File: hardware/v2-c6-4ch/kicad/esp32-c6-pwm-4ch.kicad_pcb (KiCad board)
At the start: 2 copper layers, 90 x 70 mm, 40 parts, among them Q1 AO3400A, Q2 AO3400A, Q3 AO3400A, Q4 AO3400A

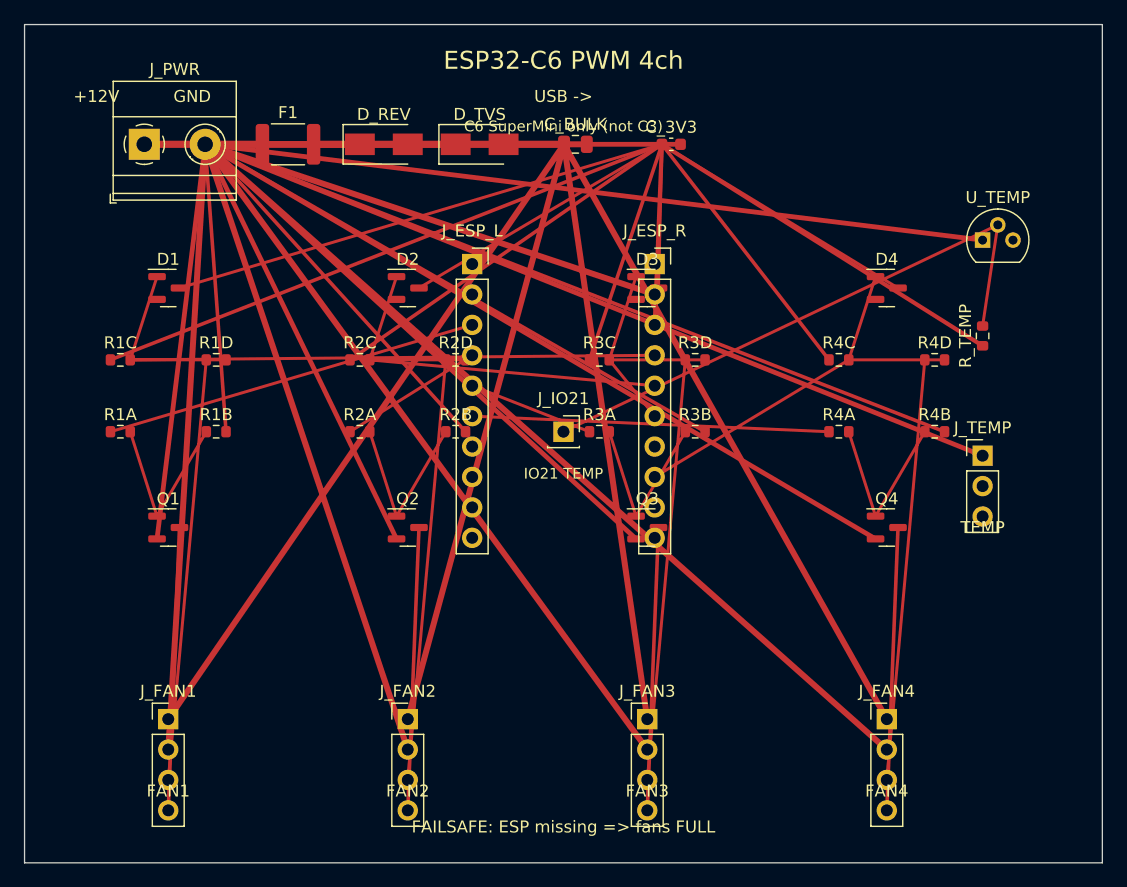
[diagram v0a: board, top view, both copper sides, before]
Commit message: no-mistakes(review): Sensorbus dokumentiert; vollständiges PCB-Routing bleibt offen
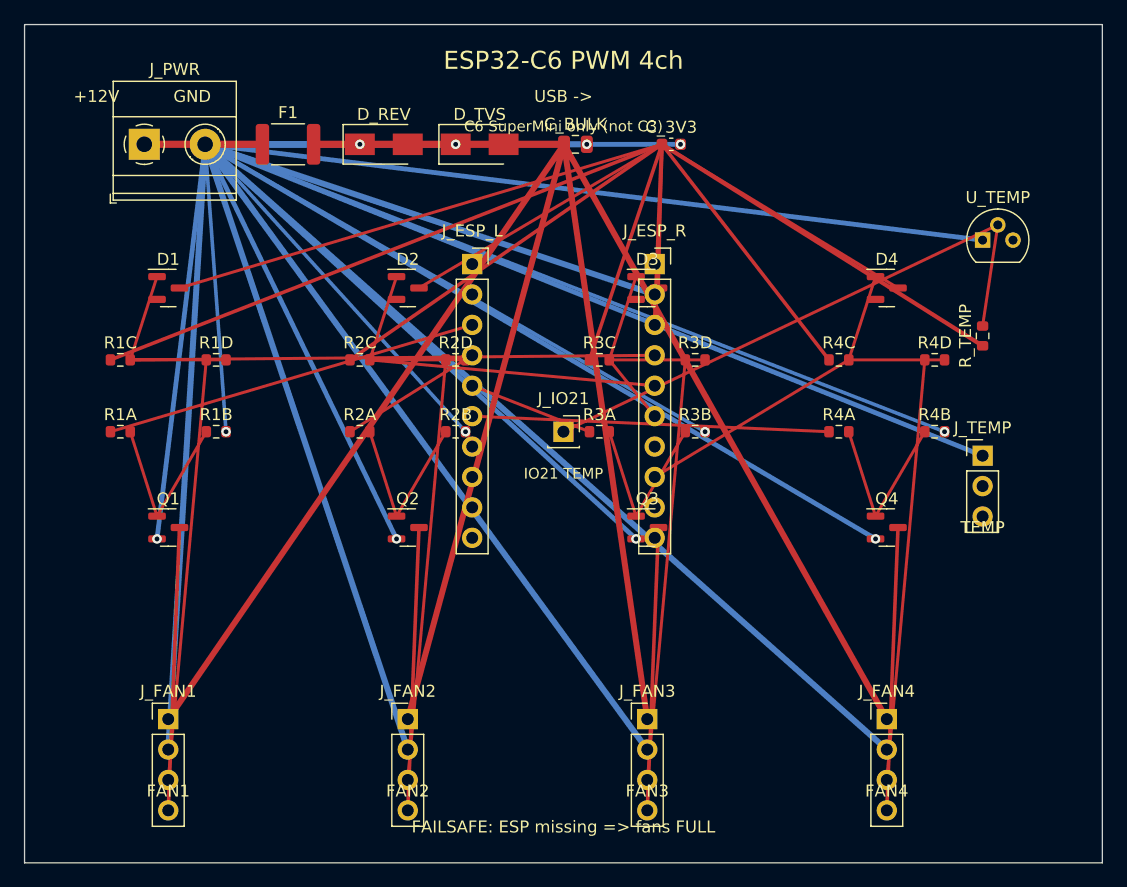
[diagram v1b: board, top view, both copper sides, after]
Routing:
- net GND: vias 0 -> 20

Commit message: no-mistakes(review): J_TEMP verbunden; 37 F.Cu-Kreuzungen bleiben offen
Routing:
- net +3V3: track 270.3 -> 346.1 mm, vias 0 -> 1
- net GND: track 877.4 -> 843.5 mm, vias 20 -> 16
- net +12V_F: track 232.5 -> 199.9 mm, vias 0 -> 1
- net TEMP_DQ: track 48.7 -> 68.1 mm
